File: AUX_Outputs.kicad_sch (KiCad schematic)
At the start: 8 parts, among them J18 AUX1 Notecard, J19 AUX2 LiDAR, J20 AUX3 GNSS, J21 AUX4 IMU

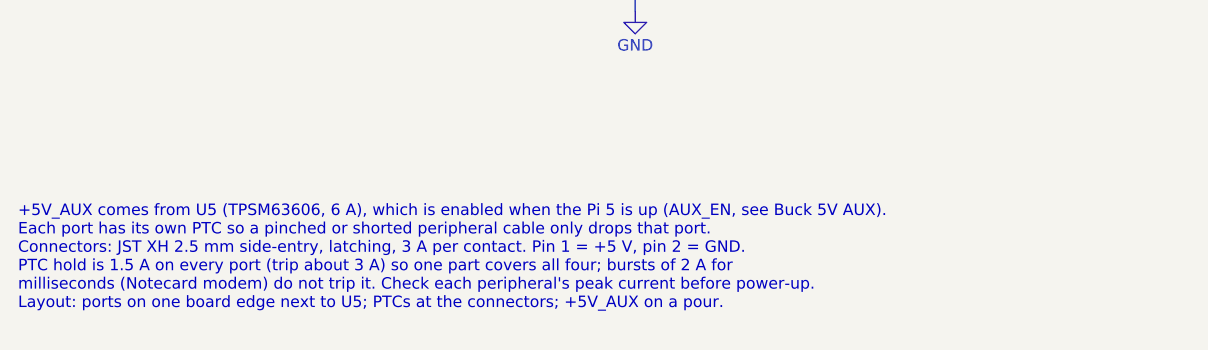
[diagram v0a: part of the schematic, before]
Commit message: Switch AUX ports to top-entry JST XH; drop encoder pull-ups and Pi sense
- J18-J21 (peripheral 5 V ports) are now top-entry JST XH B2B-XH-A:
  cables plug in from above, which suits a flat board you reach into,
  and the footprint drops from 107 to 58 mm2 per port. Use pre-made
  2-pin XH cables, so no crimping.
- Remove the DNP encoder pull-ups R48-R51. If the am-3651 outputs turn
  out to be open-collector, bodge 4.7k from each A/B line to ENCn_5V
  (noted on the Motor Control sheet).
- Remove the Pi-alive sense R44/R45. PA1 is a spare pin again (J8 pin
  2); the Pi's 3V3 on J13 still enables the AUX buck through D15.
- Board: same edits as Update PCB from Schematic (J18-J21 swapped,
  six resistors deleted, PA1 net restored on U1/J8); the parked parts
  are re-grouped beside the board. Venya's tracks unchanged (87).
- Docs, README and schematic PDF updated.

ERC 0/0. DRC: 0 errors, 3 existing text-size warnings, parity clean.
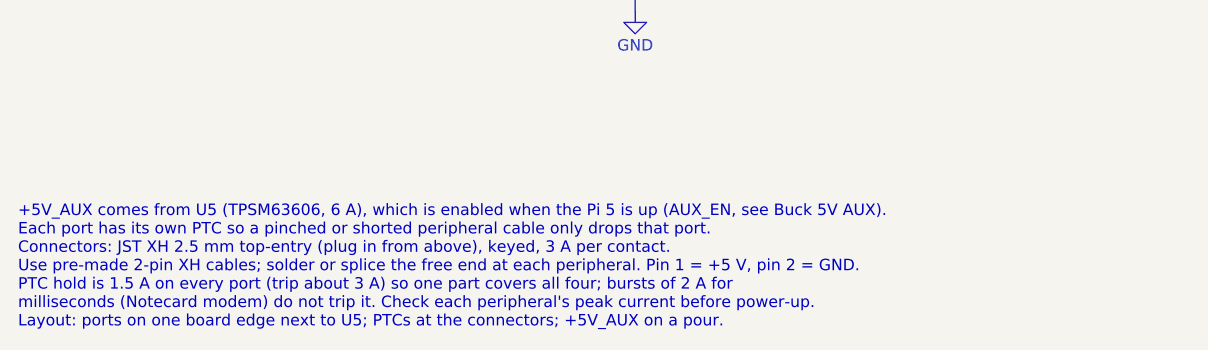
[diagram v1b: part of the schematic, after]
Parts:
- J18, J19, J20, J21: footprint Connector_JST:JST_XH_S2B-XH-A_1x02_P2.50mm_Horizontal -> Connector_JST:JST_XH_B2B-XH-A_1x02_P2.50mm_Vertical; MPN S2B-XH-A(LF)(SN) -> B2B-XH-A(LF)(SN); Mating XHP-2 housing + 2x SXH-001T-P0.6 crimp (AWG 28-22) -> Pre-made 2-pin JST XH cable (XHP-2 housing); no crimping ne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
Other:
- note added: "+5V_AUX comes from U5 (TPSM63606, 6 A), which is enabled when the Pi 5 is up (AUX_EN, see Buck 5V AUX). Each port has its own PTC so a pinched or shorted peripheral cable only drops that port. Connectors: JST XH 2.5 mm top-entry (plug in from above), keyed, 3 A per contact. Use pre-made 2-pin XH cables; solder or splice the free end at each peripheral. Pin 1 = +5 V, pin 2 = GND. PTC hold is 1.5 A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"
- note removed: "+5V_AUX comes from U5 (TPSM63606, 6 A), which is enabled when the Pi 5 is up (AUX_EN, see Buck 5V AUX). Each port has its own PTC so a pinched or shorted peripheral cable only drops that port. Connectors: JST XH 2.5 mm side-entry, latching, 3 A per contact. Pin 1 = +5 V, pin 2 = GND. PTC hold is 1.5 A on every port (trip about 3 A) so one part covers all four; bursts of 2 A for milliseconds (Note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"
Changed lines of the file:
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@@
 		)
 	)
-	(text "+5V_AUX comes from U5 (TPSM63606, 6 A), which is enabled when the Pi 5 is up (AUX_EN, see Buck 5V AUX).\nEach port has its own PTC so a pinched or shorted peripheral cable only drops that port.\nConnectors: JST XH 2.5 mm side-entry, latching, 3 A per contact. Pin 1 = +5 V, pin 2 = GND.\nPTC hold is 1.5 A on every port (trip about 3 A) so one part covers all four; bursts of 2 A for\nmilliseconds (Notecard modem) do not trip it. Check each peripheral's peak current before power-up.\nLayout: ports on one board edge next to U5; PTCs at the connectors; +5V_AUX on a pour."
+	(text "+5V_AUX comes from U5 (TPSM63606, 6 A), which is enabled when the Pi 5 is up (AUX_EN, see Buck 5V AUX).\nEach port has its own PTC so a pinched or shorted peripheral cable only drops that port.\nConnectors: JST XH 2.5 mm top-entry (plug in from above), keyed, 3 A per contact.\nUse pre-made 2-pin XH cables; solder or splice the free end at each peripheral. Pin 1 = +5 V, pin 2 = GND.\nPTC hold is 1.5 A on every port (trip about 3 A) so one part covers all four; bursts of 2 A for\nmilliseconds (Notecard modem) do not trip it. Check each peripheral's peak current before power-up.\nLayout: ports on one board edge next to U5; PTCs at the connectors; +5V_AUX on a pour."
 		(exclude_from_sim no)
 		(at 25.4 147.32 0)
@@
 			)
 		)
-		(property "Footprint" "Connector_JST:JST_XH_S2B-XH-A_1x02_P2.50mm_Horizontal"
+		(property "Footprint" "Connector_JST:JST_XH_B2B-XH-A_1x02_P2.50mm_Vertical"
 			(at 104.14 96.52 0)
 			(hide yes)
@@
 			)
 		)
-		(property "Description" "5 V output to GNSS receiver. JST XH side-entry: 1 = +5 V (AUX3_5V), 2 = GND. Mates with XHP-2 housing."
+		(property "Description" "5 V output to GNSS receiver. JST XH top-entry (plugs in from above): 1 = +5 V (AUX3_5V), 2 = GND. Use a pre-made 2-pin XH cable."
 			(at 104.14 96.52 0)
 			(hide yes)
@@
 			)
 		)
-		(property "MPN" "S2B-XH-A(LF)(SN)"
+		(property "MPN" "B2B-XH-A(LF)(SN)"
 			(at 104.14 96.52 0)
 			(hide yes)
@@
 			)
 		)
-		(property "Mating" "XHP-2 housing + 2x SXH-001T-P0.6 crimp (AWG 28-22)"
+		(property "Mating" "Pre-made 2-pin JST XH cable (XHP-2 housing); no crimping needed"
 			(at 104.14 96.52 0)
 			(hide yes)
@@
 			)
 		)
-		(property "Footprint" "Connector_JST:JST_XH_S2B-XH-A_1x02_P2.50mm_Horizontal"
+		(property "Footprint" "Connector_JST:JST_XH_B2B-XH-A_1x02_P2.50mm_Vertical"
 			(at 104.14 119.38 0)
 			(hide yes)
@@
 			)
 		)
-		(property "Description" "5 V output to BNO085 IMU board (has its own 3.3 V regulator). JST XH side-entry: 1 = +5 V (AUX4_5V), 2 = GND. Mates with XHP-2 housing."
+		(property "Description" "5 V output to BNO085 IMU board (has its own 3.3 V regulator). JST XH top-entry (plugs in from above): 1 = +5 V (AUX4_5V), 2 = GND. Use a pre-made 2-pin XH cable."
 			(at 104.14 119.38 0)
 			(hide yes)
@@
 			)
 		)
-		(property "MPN" "S2B-XH-A(LF)(SN)"
+		(property "MPN" "B2B-XH-A(LF)(SN)"
 			(at 104.14 119.38 0)
 			(hide yes)
@@
 			)
 		)
-		(property "Mating" "XHP-2 housing + 2x SXH-001T-P0.6 crimp (AWG 28-22)"
+		(property "Mating" "Pre-made 2-pin JST XH cable (XHP-2 housing); no crimping needed"
 			(at 104.14 119.38 0)
 			(hide yes)
@@
 			)
 		)
-		(property "Footprint" "Connector_JST:JST_XH_S2B-XH-A_1x02_P2.50mm_Horizontal"
+		(property "Footprint" "Connector_JST:JST_XH_B2B-XH-A_1x02_P2.50mm_Vertical"
 			(at 104.14 50.8 0)
 			(hide yes)
@@
 			)
 		)
-		(property "Description" "5 V output to Blues Notecard (cellular bursts up to about 2 A). JST XH side-entry: 1 = +5 V (AUX1_5V), 2 = GND. Mates with XHP-2 housing."
+		(property "Description" "5 V output to Blues Notecard (cellular bursts up to about 2 A). JST XH top-entry (plugs in from above): 1 = +5 V (AUX1_5V), 2 = GND. Use a pre-made 2-pin XH cable."
 			(at 104.14 50.8 0)
 			(hide yes)
@@
 			)
 		)
-		(property "MPN" "S2B-XH-A(LF)(SN)"
+		(property "MPN" "B2B-XH-A(LF)(SN)"
 			(at 104.14 50.8 0)
 			(hide yes)
@@
 			)
 		)
-		(property "Mating" "XHP-2 housing + 2x SXH-001T-P0.6 crimp (AWG 28-22)"
+		(property "Mating" "Pre-made 2-pin JST XH cable (XHP-2 housing); no crimping needed"
 			(at 104.14 50.8 0)
 			(hide yes)
@@
 			)
 		)
-		(property "Footprint" "Connector_JST:JST_XH_S2B-XH-A_1x02_P2.50mm_Horizontal"
+		(property "Footprint" "Connector_JST:JST_XH_B2B-XH-A_1x02_P2.50mm_Vertical"
 			(at 104.14 73.66 0)
 			(hide yes)
@@
 			)
 		)
-		(property "Description" "5 V output to LiDAR (motor start-up current about 1 A). JST XH side-entry: 1 = +5 V (AUX2_5V), 2 = GND. Mates with XHP-2 housing."
+		(property "Description" "5 V output to LiDAR (motor start-up current about 1 A). JST XH top-entry (plugs in from above): 1 = +5 V (AUX2_5V), 2 = GND. Use a pre-made 2-pin XH cable."
 			(at 104.14 73.66 0)
 			(hide yes)
@@
 			)
 		)
-		(property "MPN" "S2B-XH-A(LF)(SN)"
+		(property "MPN" "B2B-XH-A(LF)(SN)"
 			(at 104.14 73.66 0)
 			(hide yes)
@@
 			)
 		)
-		(property "Mating" "XHP-2 housing + 2x SXH-001T-P0.6 crimp (AWG 28-22)"
+		(property "Mating" "Pre-made 2-pin JST XH cable (XHP-2 housing); no crimping needed"
 			(at 104.14 73.66 0)
 			(hide yes)
